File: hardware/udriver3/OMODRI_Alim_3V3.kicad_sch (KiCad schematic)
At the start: 10 parts, among them U3 MPM3804GG

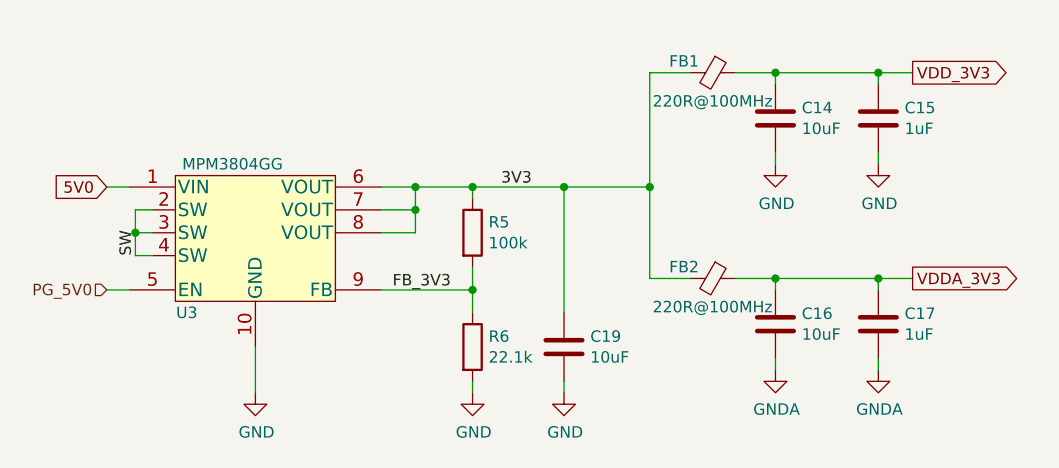
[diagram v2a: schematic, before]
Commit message: Temporary version of udrive3 v2.0. - In schematic there are 2 solutions for DC/DC buck converter. - PCB routing is not finished yet.
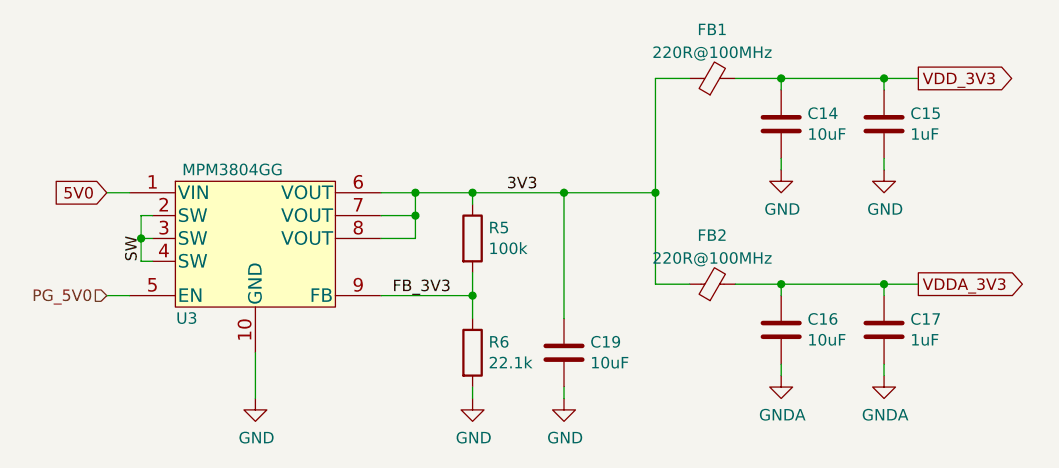
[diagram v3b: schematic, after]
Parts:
- removed FB1, FB2: 220R@100MHz, Inductor_SMD:L_0603_1608Metric, symbol omodri_laas-rescue:Ferrite_Bead_Small-Device
- added FB1, FB2: 220R@100MHz, Inductor_SMD:L_0603_1608Metric, symbol Device:FerriteBead_Small
- C14, C16, C19: footprint Capacitor_SMD:C_0603_1608Metric -> Capacitor_SMD:C_0402_1005Metric; DigiKey 490-10475-1-ND -> 490-13238-2-ND; Farnell 2456110 -> 3582794; Mouser 81-GRM188R61A106ME9D -> 81-GRM155R60J106ME5D; Part No GRM188R61A106ME69D -> GRM155R60J106ME15D; RS 113-8702 -> (none); Rated Voltage 10V -> 6.3V
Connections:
- net 3V3: now also FB1.1, FB2.1
- net VDDA_3V3: now also FB2.2
- net VDD_3V3: now also FB1.2
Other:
- moved on the sheet: C14, C15, C16, C17, C19, R5, R6, U3

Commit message: PCB update. Re-annotation of the design + via stitching (GND).
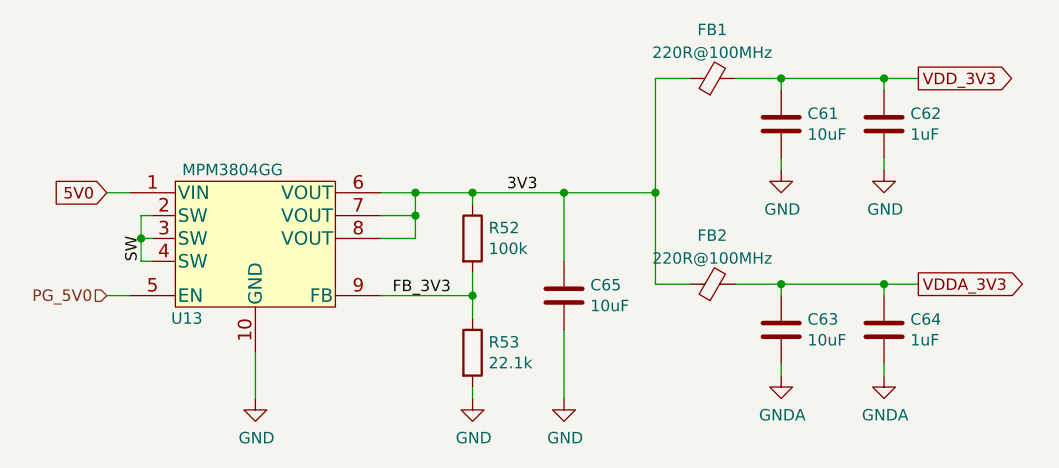
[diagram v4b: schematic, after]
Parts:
- renumbered C14 to C61, C15 to C62, C16 to C63, C17 to C64, C19 to C65, R5 to R52, R6 to R53, U3 to U13
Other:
- moved on the sheet: C65
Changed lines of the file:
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@@
     (stroke (width 0) (type default) (color 0 0 0 0))
   )
-  (wire (pts (xy 147.32 87.63) (xy 147.32 101.6))
+  (wire (pts (xy 147.32 87.63) (xy 147.32 95.25))
     (stroke (width 0) (type default) (color 0 0 0 0))
   )
@@
     (stroke (width 0) (type default) (color 0 0 0 0))
   )
+  (wire (pts (xy 147.32 102.87) (xy 147.32 110.49))
+    (stroke (width 0) (type default) (color 0 0 0 0))
+  )
   (wire (pts (xy 100.33 92.71) (xy 101.6 92.71))
-    (stroke (width 0) (type default) (color 0 0 0 0))
-  )
-  (wire (pts (xy 147.32 110.49) (xy 147.32 109.22))
     (stroke (width 0) (type default) (color 0 0 0 0))
   )
@@
   (symbol (lib_id "power:GND") (at 113.03 110.49 0) (unit 1)
     (in_bom yes) (on_board yes)
-    (property "Reference" "#PWR028" (id 0) (at 113.03 116.84 0)
+    (property "Reference" "#PWR0135" (id 0) (at 113.03 116.84 0)
       (effects (font (size 1.27 1.27)) hide)
     )
@@
   (symbol (lib_id "power:GND") (at 147.32 110.49 0) (unit 1)
     (in_bom yes) (on_board yes)
-    (property "Reference" "#PWR030" (id 0) (at 147.32 116.84 0)
+    (property "Reference" "#PWR0137" (id 0) (at 147.32 116.84 0)
       (effects (font (size 1.27 1.27)) hide)
     )
@@
   (symbol (lib_id "power:GND") (at 137.16 110.49 0) (unit 1)
     (in_bom yes) (on_board yes)
-    (property "Reference" "#PWR029" (id 0) (at 137.16 116.84 0)
+    (property "Reference" "#PWR0136" (id 0) (at 137.16 116.84 0)
       (effects (font (size 1.27 1.27)) hide)
     )
@@
   (symbol (lib_id "Device:R") (at 137.16 92.71 0) (unit 1)
     (in_bom yes) (on_board yes)
-    (property "Reference" "R5" (id 0) (at 138.938 91.5416 0)
+    (property "Reference" "R52" (id 0) (at 138.938 91.5416 0)
       (effects (font (size 1.27 1.27)) (justify left))
     )
@@
   (symbol (lib_id "Device:R") (at 137.16 105.41 0) (unit 1)
     (in_bom yes) (on_board yes)
-    (property "Reference" "R6" (id 0) (at 138.938 104.2416 0)
+    (property "Reference" "R53" (id 0) (at 138.938 104.2416 0)
       (effects (font (size 1.27 1.27)) (justify left))
     )
@@
   (symbol (lib_id "omodri_lib:MPM3804GG") (at 113.03 93.98 0) (unit 1)
     (in_bom yes) (on_board yes)
-    (property "Reference" "U3" (id 0) (at 105.41 101.6 0))
+    (property "Reference" "U13" (id 0) (at 105.41 101.6 0))
     (property "Value" "MPM3804GG" (id 1) (at 110.49 85.09 0))
     (property "Footprint" "udriver3:QFN-10_2x2mm_P0.5mm" (id 2) (at 113.03 93.98 0)
@@
     (pin "9")
   )
-  (symbol (lib_id "Device:C") (at 147.32 105.41 0) (unit 1)
-    (in_bom yes) (on_board yes)
-    (property "Reference" "C19" (id 0) (at 150.241 104.2416 0)
-      (effects (font (size 1.27 1.27)) (justify left))
-    )
-    (property "Value" "10uF" (id 1) (at 150.241 106.553 0)
-      (effects (font (size 1.27 1.27)) (justify left))
-    )
-    (property "Footprint" "Capacitor_SMD:C_0402_1005Metric" (id 2) (at 148.2852 109.22 0)
-      (effects (font (size 1.27 1.27)) hide)
-    )
-    (property "Datasheet" "~" (id 3) (at 147.32 105.41 0)
-      (effects (font (size 1.27 1.27)) hide)
-    )
-    (property "DigiKey" "490-13238-2-ND" (id 4) (at 147.32 105.41 0)
-      (effects (font (size 1.27 1.27)) hide)
-    )
-    (property "Farnell" "3582794" (id 5) (at 147.32 105.41 0)
-      (effects (font (size 1.27 1.27)) hide)
-    )
-    (property "Mouser" "81-GRM155R60J106ME5D" (id 6) (at 147.32 105.41 0)
-      (effects (font (size 1.27 1.27)) hide)
-    )
-    (property "Part No" "GRM155R60J106ME15D" (id 7) (at 147.32 105.41 0)
-      (effects (font (size 1.27 1.27)) hide)
-    )
-    (property "RS" "" (id 8) (at 147.32 105.41 0)
-      (effects (font (size 1.27 1.27)) hide)
-    )
-    (property "Rated Voltage" "6.3V" (id 9) (at 147.32 105.41 0)
+  (symbol (lib_id "Device:C") (at 147.32 99.06 0) (unit 1)
+    (in_bom yes) (on_board yes)
+    (property "Reference" "C65" (id 0) (at 150.241 97.8916 0)
+      (effects (font (size 1.27 1.27)) (justify left))
+    )
+    (property "Value" "10uF" (id 1) (at 150.241 100.203 0)
+      (effects (font (size 1.27 1.27)) (justify left))
+    )
+    (property "Footprint" "Capacitor_SMD:C_0402_1005Metric" (id 2) (at 148.2852 102.87 0)
+      (effects (font (size 1.27 1.27)) hide)
+    )
+    (property "Datasheet" "~" (id 3) (at 147.32 99.06 0)
+      (effects (font (size 1.27 1.27)) hide)
+    )
+    (property "DigiKey" "490-13238-2-ND" (id 4) (at 147.32 99.06 0)
+      (effects (font (size 1.27 1.27)) hide)
+    )
+    (property "Farnell" "3582794" (id 5) (at 147.32 99.06 0)
+      (effects (font (size 1.27 1.27)) hide)
+    )
+    (property "Mouser" "81-GRM155R60J106ME5D" (id 6) (at 147.32 99.06 0)
+      (effects (font (size 1.27 1.27)) hide)
+    )
+    (property "Part No" "GRM155R60J106ME15D" (id 7) (at 147.32 99.06 0)
+      (effects (font (size 1.27 1.27)) hide)
+    )
+    (property "RS" "" (id 8) (at 147.32 99.06 0)
+      (effects (font (size 1.27 1.27)) hide)
+    )
+    (property "Rated Voltage" "6.3V" (id 9) (at 147.32 99.06 0)
       (effects (font (size 1.27 1.27)) hide)
     )
@@
   (symbol (lib_id "Device:C") (at 171.45 80.01 0) (unit 1)
     (in_bom yes) (on_board yes)
-    (property "Reference" "C14" (id 0) (at 174.371 78.8416 0)
+    (property "Reference" "C61" (id 0) (at 174.371 78.8416 0)
       (effects (font (size 1.27 1.27)) (justify left))
     )
@@
   (symbol (lib_id "Device:C") (at 182.88 80.01 0) (unit 1)
     (in_bom yes) (on_board yes)
-    (property "Reference" "C15" (id 0) (at 185.801 78.8416 0)
+    (property "Reference" "C62" (id 0) (at 185.801 78.8416 0)
       (effects (font (size 1.27 1.27)) (justify left))
     )
@@
   (symbol (lib_id "power:GND") (at 171.45 85.09 0) (unit 1)
     (in_bom yes) (on_board yes)
-    (property "Reference" "#PWR023" (id 0) (at 171.45 91.44 0)
+    (property "Reference" "#PWR0131" (id 0) (at 171.45 91.44 0)
       (effects (font (size 1.27 1.27)) hide)
     )
@@
   (symbol (lib_id "power:GND") (at 182.88 85.09 0) (unit 1)
     (in_bom yes) (on_board yes)
-    (property "Reference" "#PWR024" (id 0) (at 182.88 91.44 0)
+    (property "Reference" "#PWR0132" (id 0) (at 182.88 91.44 0)
       (effects (font (size 1.27 1.27)) hide)
     )
@@
   (symbol (lib_id "Device:C") (at 171.45 102.87 0) (unit 1)
     (in_bom yes) (on_board yes)
-    (property "Reference" "C16" (id 0) (at 174.371 101.7016 0)
+    (property "Reference" "C63" (id 0) (at 174.371 101.7016 0)
       (effects (font (size 1.27 1.27)) (justify left))
     )
@@
   (symbol (lib_id "Device:C") (at 182.88 102.87 0) (unit 1)
     (in_bom yes) (on_board yes)
-    (property "Reference" "C17" (id 0) (at 185.801 101.7016 0)
+    (property "Reference" "C64" (id 0) (at 185.801 101.7016 0)
       (effects (font (size 1.27 1.27)) (justify left))
     )
@@
   (symbol (lib_id "power:GNDA") (at 171.45 107.95 0) (unit 1)
     (in_bom yes) (on_board yes)
-    (property "Reference" "#PWR025" (id 0) (at 171.45 114.3 0)
+    (property "Reference" "#PWR0133" (id 0) (at 171.45 114.3 0)
       (effects (font (size 1.27 1.27)) hide)
     )
@@
   (symbol (lib_id "power:GNDA") (at 182.88 107.95 0) (unit 1)
     (in_bom yes) (on_board yes)
-    (property "Reference" "#PWR026" (id 0) (at 182.88 114.3 0)
-      (effects (font (size 1.27 1.27)) hide)
-    )
+    (property "Reference" "#PWR0134" (id 0) (at 182.88 114.3 0)
+      (effects (font (size 1.27 1.27)) hide)
+    )

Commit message: PCB updates. - Replace CAN/RS485 120ohm resistor - Replace resistor on TCAN RXD pin - Update of some references - Add some 3D missing models
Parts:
- renumbered C65 to C63, C63 to C64, C64 to C65
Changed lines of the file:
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@@
   (symbol (lib_id "Device:C") (at 147.32 99.06 0) (unit 1)
     (in_bom yes) (on_board yes)
-    (property "Reference" "C65" (id 0) (at 150.241 97.8916 0)
+    (property "Reference" "C63" (id 0) (at 150.241 97.8916 0)
       (effects (font (size 1.27 1.27)) (justify left))
     )
@@
   (symbol (lib_id "Device:C") (at 171.45 102.87 0) (unit 1)
     (in_bom yes) (on_board yes)
-    (property "Reference" "C63" (id 0) (at 174.371 101.7016 0)
+    (property "Reference" "C64" (id 0) (at 174.371 101.7016 0)
       (effects (font (size 1.27 1.27)) (justify left))
     )
@@
   (symbol (lib_id "Device:C") (at 182.88 102.87 0) (unit 1)
     (in_bom yes) (on_board yes)
-    (property "Reference" "C64" (id 0) (at 185.801 101.7016 0)
+    (property "Reference" "C65" (id 0) (at 185.801 101.7016 0)
       (effects (font (size 1.27 1.27)) (justify left))
     )

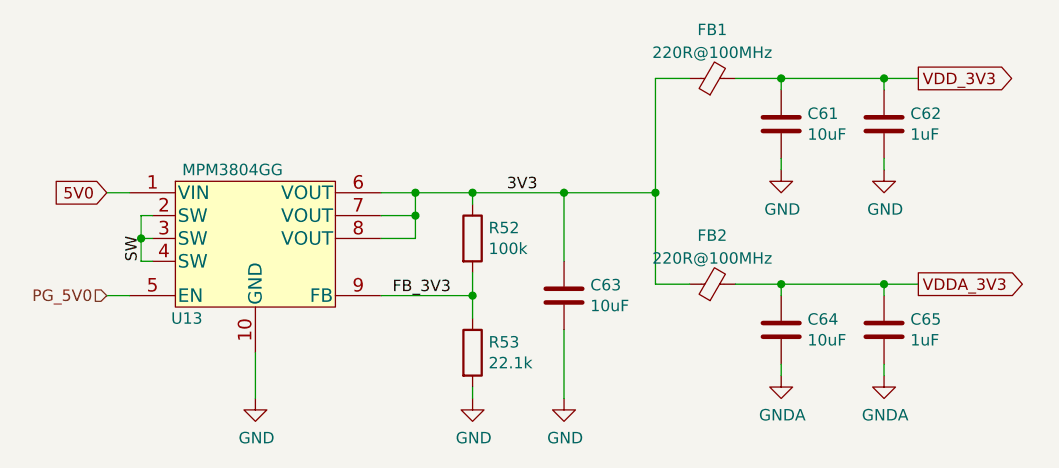
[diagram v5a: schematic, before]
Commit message: PCB updates - FSI protection added against FPC cable reverse connection - BOSCH BMI088 IMU added.
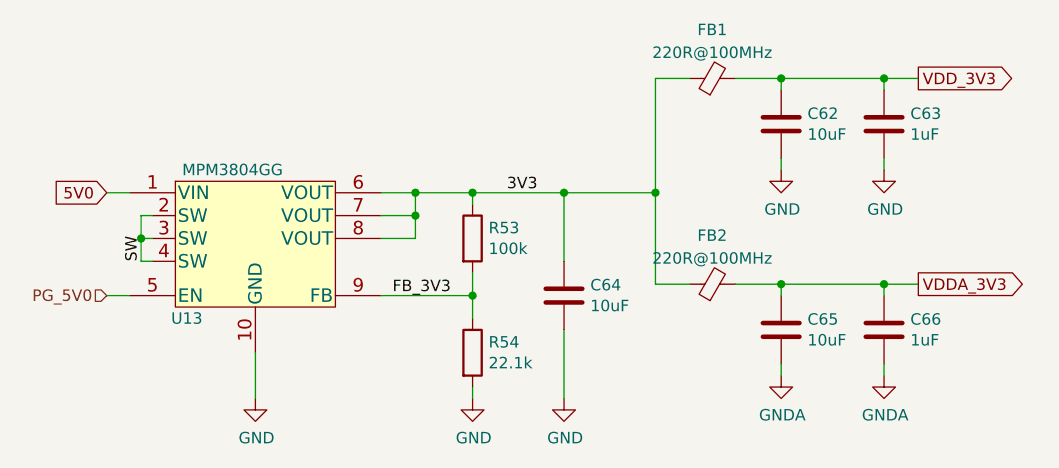
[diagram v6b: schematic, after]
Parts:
- renumbered C61 to C62, C62 to C63, C63 to C64, C64 to C65, C65 to C66, R52 to R53, R53 to R54
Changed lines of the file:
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@@
   (title_block
     (title "Open MOtor DRiver Initiative (OMODRI)")
-    (date "2022-10-05")
+    (date "2022-11-24")
     (rev "2.0")
     (company "LAAS/CNRS")
@@
   (symbol (lib_id "power:GND") (at 113.03 110.49 0) (unit 1)
     (in_bom yes) (on_board yes)
-    (property "Reference" "#PWR0135" (id 0) (at 113.03 116.84 0)
+    (property "Reference" "#PWR0136" (id 0) (at 113.03 116.84 0)
       (effects (font (size 1.27 1.27)) hide)
     )
@@
   (symbol (lib_id "power:GND") (at 147.32 110.49 0) (unit 1)
     (in_bom yes) (on_board yes)
-    (property "Reference" "#PWR0137" (id 0) (at 147.32 116.84 0)
+    (property "Reference" "#PWR0138" (id 0) (at 147.32 116.84 0)
       (effects (font (size 1.27 1.27)) hide)
     )
@@
   (symbol (lib_id "power:GND") (at 137.16 110.49 0) (unit 1)
     (in_bom yes) (on_board yes)
-    (property "Reference" "#PWR0136" (id 0) (at 137.16 116.84 0)
+    (property "Reference" "#PWR0137" (id 0) (at 137.16 116.84 0)
       (effects (font (size 1.27 1.27)) hide)
     )
@@
   (symbol (lib_id "Device:R") (at 137.16 92.71 0) (unit 1)
     (in_bom yes) (on_board yes)
-    (property "Reference" "R52" (id 0) (at 138.938 91.5416 0)
+    (property "Reference" "R53" (id 0) (at 138.938 91.5416 0)
       (effects (font (size 1.27 1.27)) (justify left))
     )
@@
   (symbol (lib_id "Device:R") (at 137.16 105.41 0) (unit 1)
     (in_bom yes) (on_board yes)
-    (property "Reference" "R53" (id 0) (at 138.938 104.2416 0)
+    (property "Reference" "R54" (id 0) (at 138.938 104.2416 0)
       (effects (font (size 1.27 1.27)) (justify left))
     )
@@
   (symbol (lib_id "Device:C") (at 147.32 99.06 0) (unit 1)
     (in_bom yes) (on_board yes)
-    (property "Reference" "C63" (id 0) (at 150.241 97.8916 0)
+    (property "Reference" "C64" (id 0) (at 150.241 97.8916 0)
       (effects (font (size 1.27 1.27)) (justify left))
     )
@@
   (symbol (lib_id "Device:C") (at 171.45 80.01 0) (unit 1)
     (in_bom yes) (on_board yes)
-    (property "Reference" "C61" (id 0) (at 174.371 78.8416 0)
+    (property "Reference" "C62" (id 0) (at 174.371 78.8416 0)
       (effects (font (size 1.27 1.27)) (justify left))
     )
@@
   (symbol (lib_id "Device:C") (at 182.88 80.01 0) (unit 1)
     (in_bom yes) (on_board yes)
-    (property "Reference" "C62" (id 0) (at 185.801 78.8416 0)
+    (property "Reference" "C63" (id 0) (at 185.801 78.8416 0)
       (effects (font (size 1.27 1.27)) (justify left))
     )
@@
   (symbol (lib_id "power:GND") (at 171.45 85.09 0) (unit 1)
     (in_bom yes) (on_board yes)
-    (property "Reference" "#PWR0131" (id 0) (at 171.45 91.44 0)
+    (property "Reference" "#PWR0132" (id 0) (at 171.45 91.44 0)
       (effects (font (size 1.27 1.27)) hide)
     )
@@
   (symbol (lib_id "power:GND") (at 182.88 85.09 0) (unit 1)
     (in_bom yes) (on_board yes)
-    (property "Reference" "#PWR0132" (id 0) (at 182.88 91.44 0)
+    (property "Reference" "#PWR0133" (id 0) (at 182.88 91.44 0)
       (effects (font (size 1.27 1.27)) hide)
     )
@@
   (symbol (lib_id "Device:C") (at 171.45 102.87 0) (unit 1)
     (in_bom yes) (on_board yes)
-    (property "Reference" "C64" (id 0) (at 174.371 101.7016 0)
+    (property "Reference" "C65" (id 0) (at 174.371 101.7016 0)
       (effects (font (size 1.27 1.27)) (justify left))
     )
@@
   (symbol (lib_id "Device:C") (at 182.88 102.87 0) (unit 1)
     (in_bom yes) (on_board yes)
-    (property "Reference" "C65" (id 0) (at 185.801 101.7016 0)
+    (property "Reference" "C66" (id 0) (at 185.801 101.7016 0)
       (effects (font (size 1.27 1.27)) (justify left))
     )
@@
   (symbol (lib_id "power:GNDA") (at 171.45 107.95 0) (unit 1)
     (in_bom yes) (on_board yes)
-    (property "Reference" "#PWR0133" (id 0) (at 171.45 114.3 0)
+    (property "Reference" "#PWR0134" (id 0) (at 171.45 114.3 0)
       (effects (font (size 1.27 1.27)) hide)
     )
@@
   (symbol (lib_id "power:GNDA") (at 182.88 107.95 0) (unit 1)
     (in_bom yes) (on_board yes)
-    (property "Reference" "#PWR0134" (id 0) (at 182.88 114.3 0)
-      (effects (font (size 1.27 1.27)) hide)
-    )
+    (property "Reference" "#PWR0135" (id 0) (at 182.88 114.3 0)
+      (effects (font (size 1.27 1.27)) hide)
+    )
